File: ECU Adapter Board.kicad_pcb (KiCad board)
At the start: 2 copper layers, 150 x 100 mm, 26 parts, among them J1 Conn_01x03_Pin, J10 Conn_01x03_Pin, J11 DSUB_15pin/VGA Veritical Fema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, J12 Conn_01x03_Pin, J13 DSUB_15pin/VGA Veritical Fema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, J14 Conn_01x03_Pin, J15 DSUB_15pin/VGA Veritical Fema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, J16 Conn_01x03_Pin, J17 DSUB_15pin/VGA Veritical Fema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, J18 Conn_01x03_Pin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

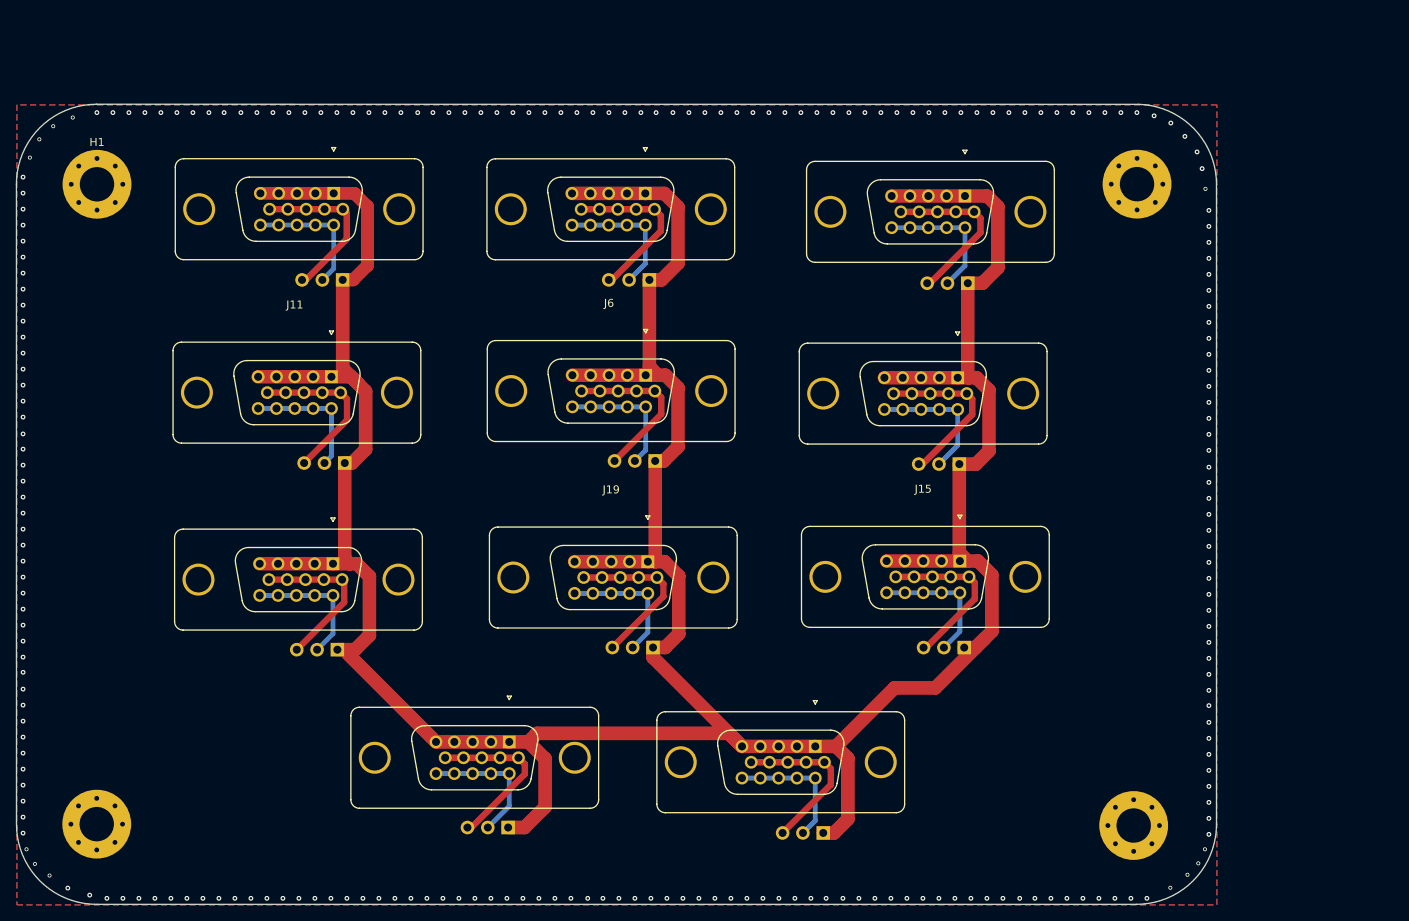
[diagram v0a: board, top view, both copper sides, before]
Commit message: removed unnecessary gnd trace
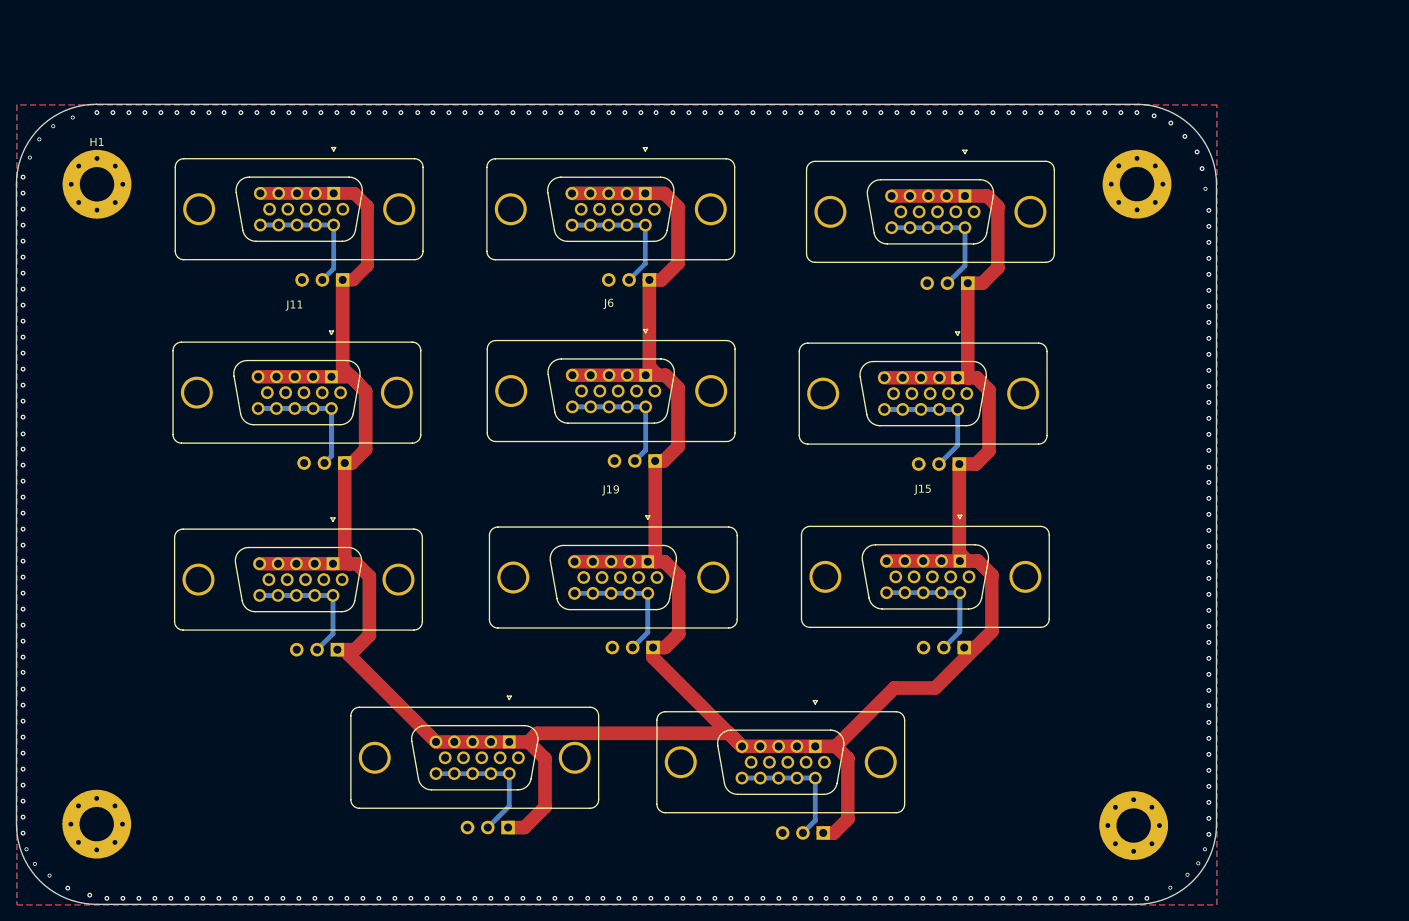
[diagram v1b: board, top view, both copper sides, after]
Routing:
- net GND: track 230.7 -> 2.86 mm

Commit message: grounded mounting holes
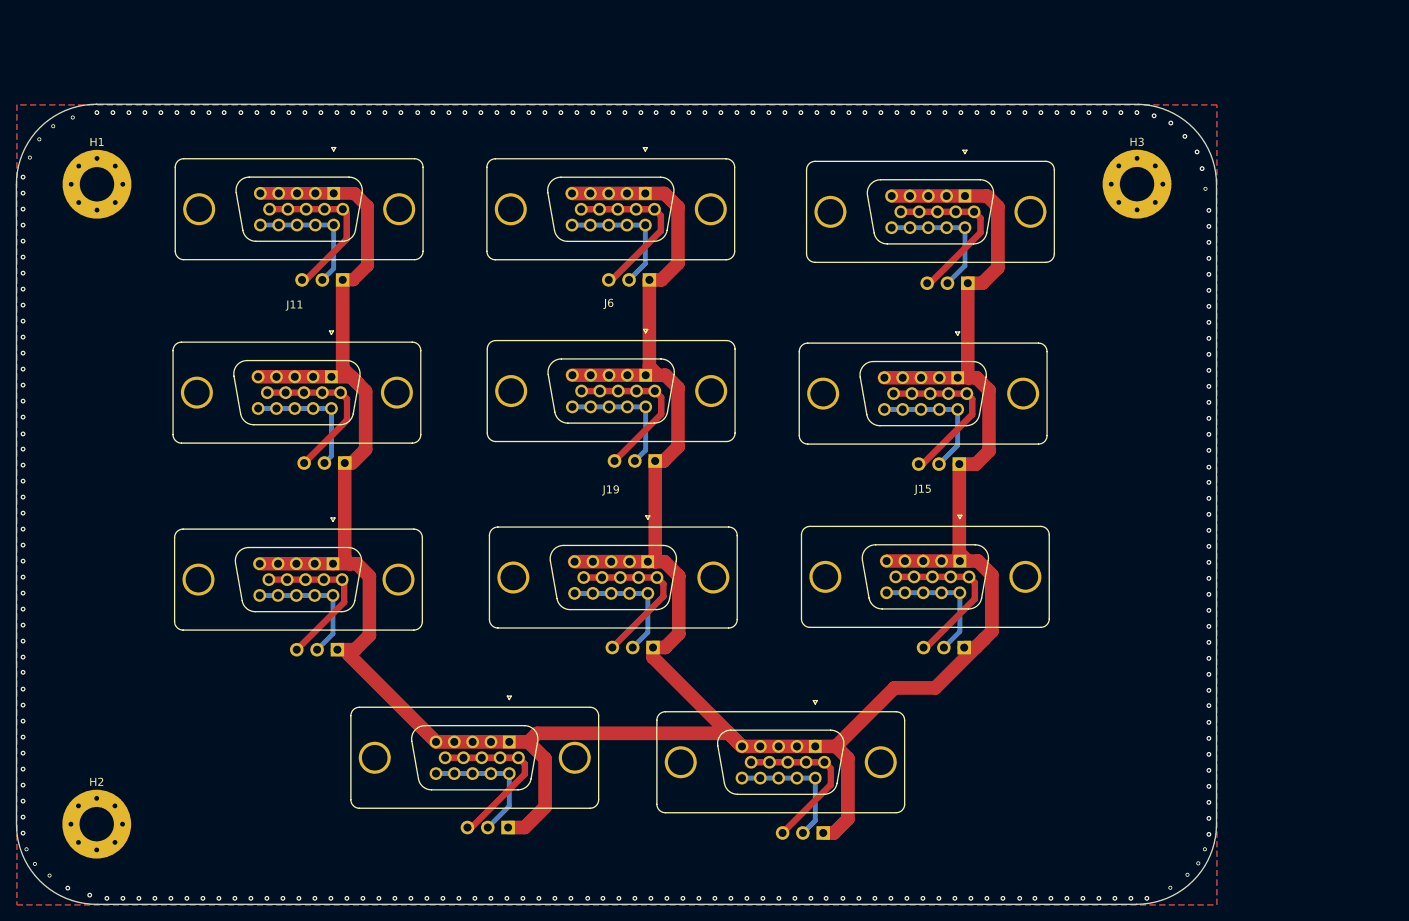
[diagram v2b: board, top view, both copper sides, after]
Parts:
- removed H5: MountingHole, MountingHole:MountingHole_4.3mm_M4_Pad_Via
- H1, H2, H3: value MountingHole -> MountingHole_Pad
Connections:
- H1 pad 1: (no net) -> GND
- H2 pad 1: (no net) -> GND
- H3 pad 1: (no net) -> GND
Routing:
- net GND: track 2.86 -> 230.7 mm

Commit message: silkscreen labeling, fixed trace thicknesses
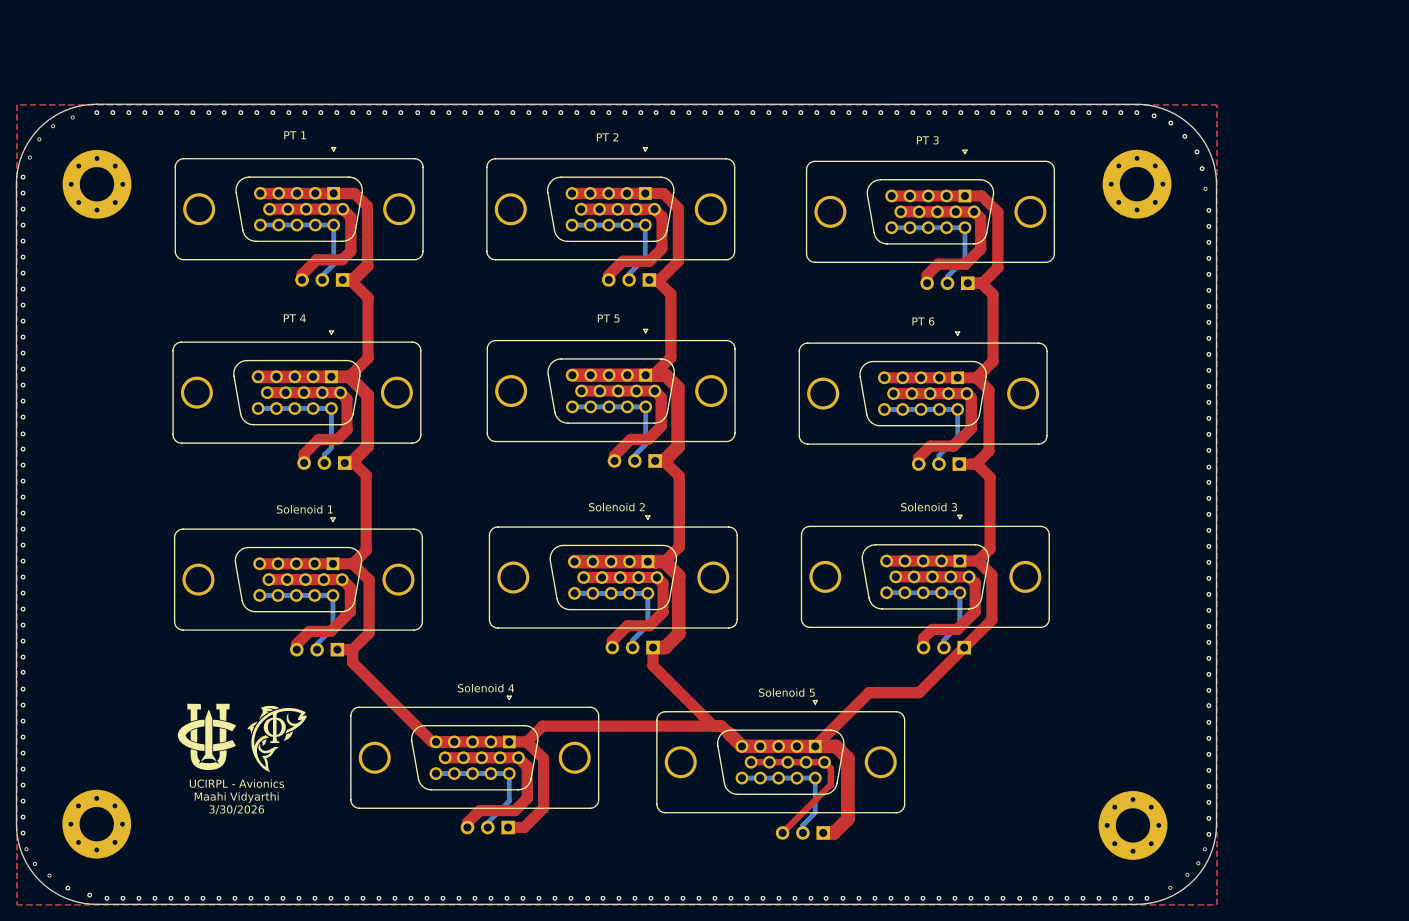
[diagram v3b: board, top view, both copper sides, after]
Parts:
- added G***: LOGO, PCB_Logo:fish logo, F.Cu at (129.0, 116.6)
- added G***: LOGO, PCB_Logo:UCIRPL_Logo, F.Cu at (120.3, 116.6)
- added H4: MountingHole_Pad, MountingHole:MountingHole_4.3mm_M4_Pad_Via, F.Cu at (236.2, 127.5)
- PT 1: renamed from J4
- PT 2: renamed from J8
- PT 3: renamed from J2
- PT 4: renamed from J11
- PT 5: renamed from J6
- PT 6: renamed from J22
- Solenoid 1: renamed from J13
- Solenoid 2: renamed from J19
- Solenoid 3: renamed from J15
- Solenoid 4: renamed from J21
- Solenoid 5: renamed from J17
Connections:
- PT 1 pad 0: unconnected-(J4-Pad0) -> GND
- PT 2 pad 0: unconnected-(J8-Pad0)_1 -> GND
- PT 3 pad 0: unconnected-(J2-Pad0)_1 -> GND
- PT 4 pad 0: unconnected-(J11-Pad0)_1 -> GND
- PT 5 pad 0: unconnected-(J6-Pad0)_1 -> GND
- PT 6 pad 0: unconnected-(J22-Pad0)_1 -> GND
- Solenoid 1 pad 0: unconnected-(J13-Pad0)_1 -> GND
- Solenoid 2 pad 0: unconnected-(J19-Pad0)_1 -> GND
- Solenoid 3 pad 0: unconnected-(J15-Pad0) -> GND
- Solenoid 4 pad 0: unconnected-(J21-Pad0) -> GND
- Solenoid 5 pad 0: unconnected-(J17-Pad0) -> GND
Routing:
- net GND: track 230.7 -> 251.3 mm
- net +24V: track 441.2 -> 454.2 mm
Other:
- board text added: "UCIRPL - Avionics Maahi Vidyarthi 3/30/2026"

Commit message: grounded pin 11 on PT Connectors
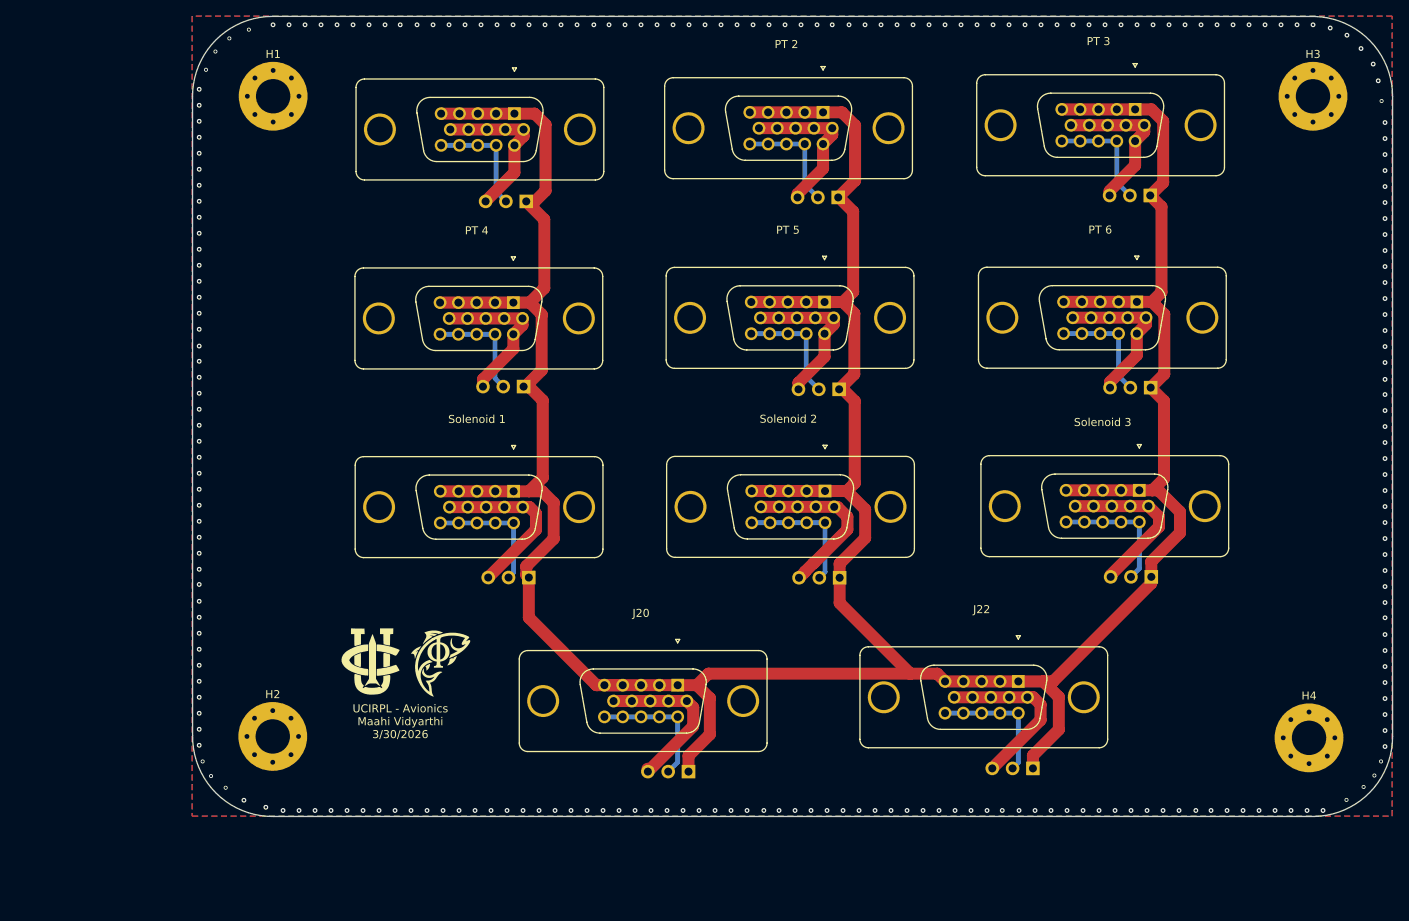
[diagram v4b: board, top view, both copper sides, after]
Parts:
- removed J10, J12, J14, J16: Conn_01x03_Pin, Connector_PinHeader_2.54mm:PinHeader_1x03_P2.54mm_Vertical
- removed PT 1: DSUB_15pin/VGA Veritical Female, UCIRP-KiCAD-Lib:Connector_VGA_Vertical
- removed Solenoid 3: DSUB_15pin/VGA Veritical Female, UCIRP-KiCAD-Lib:Connector_VGA_Vertical
- removed Solenoid 4: DSUB_15pin/VGA Veritical Female, UCIRP-KiCAD-Lib:Connector_VGA_Vertical
- removed Solenoid 5: DSUB_15pin/VGA Veritical Female, UCIRP-KiCAD-Lib:Connector_VGA_Vertical
- added J11: Conn_01x03_Pin, Connector_PinHeader_2.54mm:PinHeader_1x03_P2.54mm_Vertical, B.Cu at (238.4, 72.8)
- added J13: Conn_01x03_Pin, Connector_PinHeader_2.54mm:PinHeader_1x03_P2.54mm_Vertical, B.Cu at (160.7, 96.5)
- added J15: Conn_01x03_Pin, Connector_PinHeader_2.54mm:PinHeader_1x03_P2.54mm_Vertical, B.Cu at (199.6, 96.6)
- added J17: Conn_01x03_Pin, Connector_PinHeader_2.54mm:PinHeader_1x03_P2.54mm_Vertical, B.Cu at (238.5, 96.5)
- added J19: Conn_01x03_Pin, Connector_PinHeader_2.54mm:PinHeader_1x03_P2.54mm_Vertical, B.Cu at (180.7, 120.8)
- added J2: DSUB_15pin/VGA Veritical Female, UCIRP-KiCAD-Lib:Connector_VGA_Vertical, F.Cu at (154.3, 30.0)
- added J21: Conn_01x03_Pin, Connector_PinHeader_2.54mm:PinHeader_1x03_P2.54mm_Vertical, B.Cu at (223.7, 120.4)
- added J22: DSUB_15pin/VGA Veritical Female, UCIRP-KiCAD-Lib:Connector_VGA_Vertical, F.Cu at (217.3, 101.0)
- J18, J20: value Conn_01x03_Pin -> DSUB_15pin/VGA Veritical Female; footprint Connector_PinHeader_2.54mm:PinHeader_1x03_P2.54mm_Vertical -> UCIRP-KiCAD-Lib:Connector_VGA_Vertical; moved to F.Cu
- moved J9 70.7 mm to (199.5, 73.0)
- moved J5 70.2 mm to (238.4, 48.8)
- moved J18 62.9 mm to (232.4, 77.1), turned to 0 degrees
- moved J3 62.8 mm to (199.4, 49.0)
- moved J1 56.1 mm to (160.4, 49.5)
- moved J20 31.1 mm to (174.7, 101.5), turned to 0 degrees
- moved H1 24.6 mm to (128.7, 36.4)
- moved H3 24.6 mm to (258.7, 36.4)
- moved H2 24.6 mm to (128.7, 116.4)
- moved H4 24.6 mm to (258.2, 116.6)
- moved PT 4 24.6 mm to (154.2, 53.7)
- moved PT 2 24.4 mm to (192.9, 29.9)
- moved PT 6 24.3 mm to (232.1, 53.6)
- moved Solenoid 1 24.3 mm to (154.2, 77.2)
- moved PT 5 24.2 mm to (193.1, 53.6)
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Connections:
- J1 pad 2: Net-(J1-Pin_2) -> /PT1/SIG_OUT
- J18 pad 2: Net-(J18-Pin_2) -> +24V
- J18 pad 3: GND -> +24V
- J20 pad 2: Net-(J20-Pin_2) -> +24V
- J20 pad 3: GND -> +24V
- J3 pad 2: Net-(J3-Pin_2) -> /PT2/SIG_OUT
- J5 pad 2: Net-(J5-Pin_2) -> /PT3/SIG_OUT
- J7 pad 2: Net-(J7-Pin_2) -> /PT4/SIG_OUT
- J9 pad 2: Net-(J9-Pin_2) -> /PT5/SIG_OUT
- PT 2 pad 11: Net-(J7-Pin_2) -> GND
- PT 2 pad 12: Net-(J7-Pin_2) -> /PT2/SIG_OUT
- PT 2 pad 13: Net-(J7-Pin_2) -> /PT2/SIG_OUT
- PT 2 pad 14: Net-(J7-Pin_2) -> /PT2/SIG_OUT
- PT 2 pad 15: Net-(J7-Pin_2) -> /PT2/SIG_OUT
- PT 3 pad 11: Net-(J1-Pin_2) -> GND
- PT 3 pad 12: Net-(J1-Pin_2) -> /PT3/SIG_OUT
- PT 3 pad 13: Net-(J1-Pin_2) -> /PT3/SIG_OUT
- PT 3 pad 14: Net-(J1-Pin_2) -> /PT3/SIG_OUT
- PT 3 pad 15: Net-(J1-Pin_2) -> /PT3/SIG_OUT
- PT 4 pad 11: Net-(J10-Pin_2) -> GND
- PT 4 pad 12: Net-(J10-Pin_2) -> /PT4/SIG_OUT
- PT 4 pad 13: Net-(J10-Pin_2) -> /PT4/SIG_OUT
- PT 4 pad 14: Net-(J10-Pin_2) -> /PT4/SIG_OUT
- PT 4 pad 15: Net-(J10-Pin_2) -> /PT4/SIG_OUT
- PT 5 pad 11: Net-(J5-Pin_2) -> GND
- PT 5 pad 12: Net-(J5-Pin_2) -> /PT5/SIG_OUT
- PT 5 pad 13: Net-(J5-Pin_2) -> /PT5/SIG_OUT
- PT 5 pad 14: Net-(J5-Pin_2) -> /PT5/SIG_OUT
- PT 5 pad 15: Net-(J5-Pin_2) -> /PT5/SIG_OUT
- PT 6 pad 11: Net-(J12-Pin_2) -> GND
- PT 6 pad 12: Net-(J12-Pin_2) -> /PT6/SIG_OUT
- PT 6 pad 13: Net-(J12-Pin_2) -> /PT6/SIG_OUT
- PT 6 pad 14: Net-(J12-Pin_2) -> /PT6/SIG_OUT
- PT 6 pad 15: Net-(J12-Pin_2) -> /PT6/SIG_OUT
- Solenoid 1 pad 11: Net-(J9-Pin_2) -> /Solenoid 1/SIG_OUT
- Solenoid 1 pad 12: Net-(J9-Pin_2) -> /Solenoid 1/SIG_OUT
- Solenoid 1 pad 13: Net-(J9-Pin_2) -> /Solenoid 1/SIG_OUT
- Solenoid 1 pad 14: Net-(J9-Pin_2) -> /Solenoid 1/SIG_OUT
- Solenoid 1 pad 15: Net-(J9-Pin_2) -> /Solenoid 1/SIG_OUT
- Solenoid 2 pad 11: Net-(J18-Pin_2) -> /Solenoid 2/SIG_OUT
- Solenoid 2 pad 12: Net-(J18-Pin_2) -> /Solenoid 2/SIG_OUT
- Solenoid 2 pad 13: Net-(J18-Pin_2) -> /Solenoid 2/SIG_OUT
- Solenoid 2 pad 14: Net-(J18-Pin_2) -> /Solenoid 2/SIG_OUT
- Solenoid 2 pad 15: Net-(J18-Pin_2) -> /Solenoid 2/SIG_OUT
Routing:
- net GND: track 251.3 -> 225.3 mm
- net Net-(J20-Pin_2): track 17.0 -> 0.00 mm
- net Net-(J1-Pin_2): track 17.0 -> 0.00 mm
- net Net-(J12-Pin_2): track 17.0 -> 0.00 mm
- net Net-(J7-Pin_2): track 16.9 -> 0.00 mm
- net Net-(J14-Pin_2): track 16.8 -> 0.00 mm
- net Net-(J9-Pin_2): track 16.8 -> 0.00 mm
- net Net-(J18-Pin_2): track 16.7 -> 0.00 mm
- net Net-(J16-Pin_2): track 16.7 -> 0.00 mm
- net Net-(J3-Pin_2): track 16.6 -> 0.00 mm
- net /Solenoid 4/SIG_OUT: track 0.00 -> 16.5 mm
- net Net-(J5-Pin_2): track 16.5 -> 0.00 mm
- net /Solenoid 3/SIG_OUT: track 0.00 -> 16.5 mm
- net /Solenoid 5/SIG_OUT: track 0.00 -> 16.4 mm
- net Net-(J10-Pin_2): track 16.3 -> 0.00 mm
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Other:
- outline, holes or cut-outs redrawn
- board text added: "Solenoid 3"
